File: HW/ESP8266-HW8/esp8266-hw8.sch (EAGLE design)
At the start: 28 parts, among them IC1 MCP1703CB, J2 Sensors2, J3 Analog, J4 Sensors1, J5 Enable, J6 PGM, J9 Pwr sw, T1 BSS138, U1 ESP07-16PIN, U2 2479

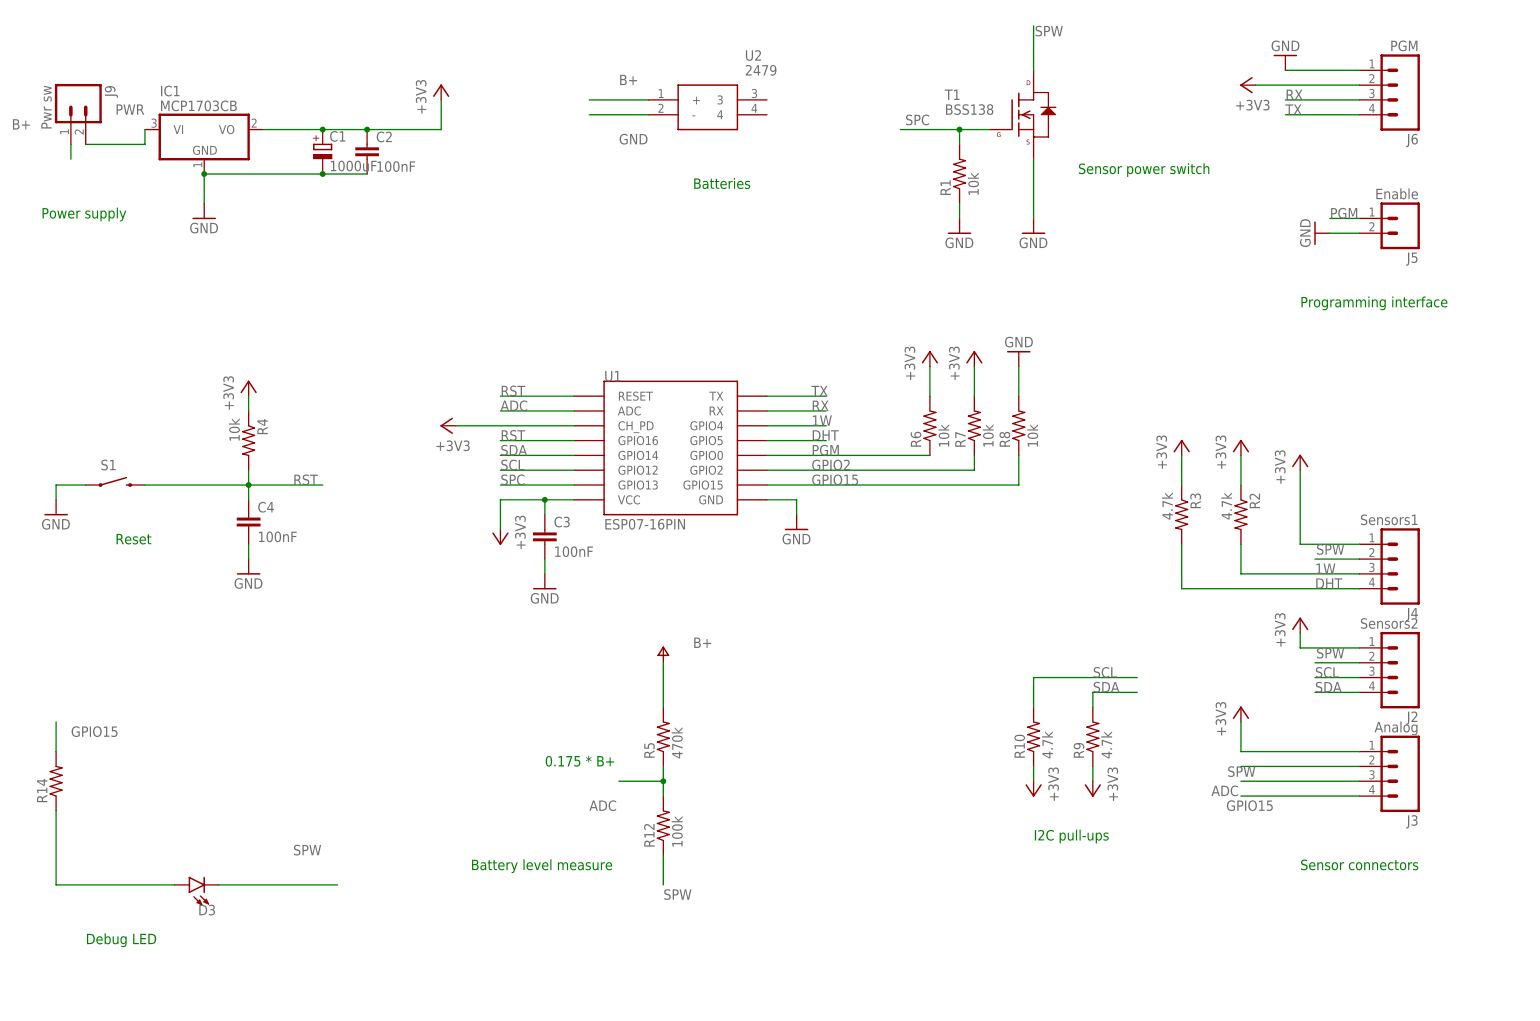
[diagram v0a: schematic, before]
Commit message: New pcb releases and some updated software
New (final?) releases of pcbs for version 7 and 8. New test program to run for test of the built hardware.
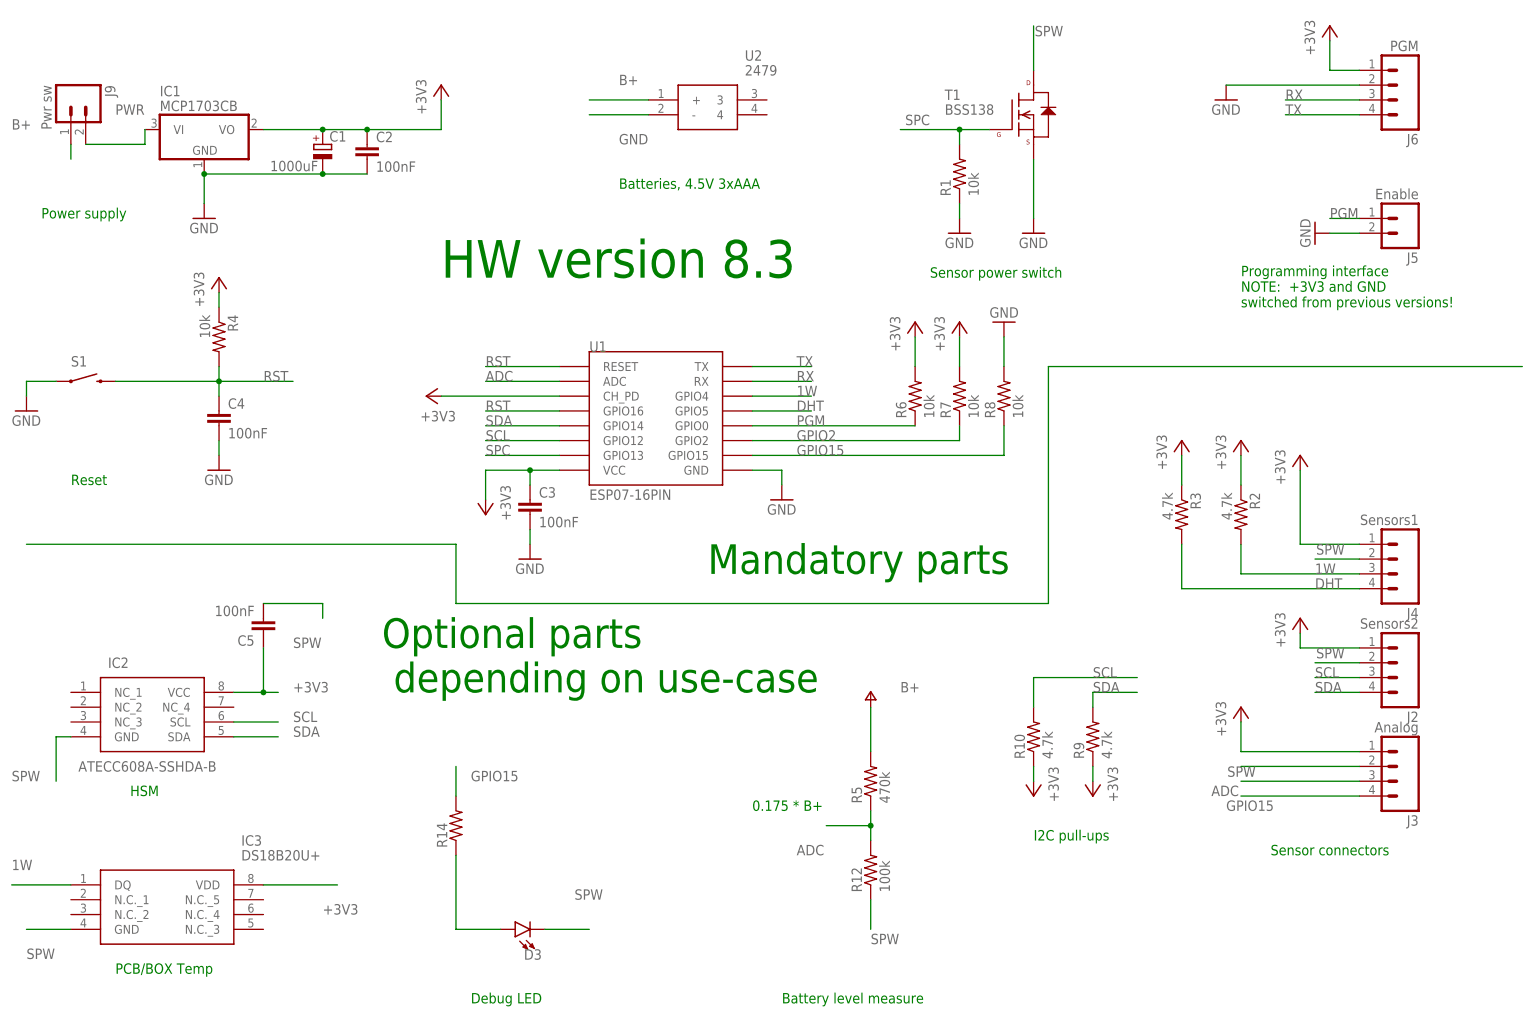
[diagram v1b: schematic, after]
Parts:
- added C5: 100nF, SparkFun-Passives:CAP0805
- added IC2: ATECC608A-SSHDA-B, SamacSys_Parts:ATECC608A-SSHDA-B
- added IC3: DS18B20U+, SamacSys_Parts:DS18B20U+
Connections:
- net +3V3: now also C5.1, IC2.VCC, IC3.VDD, J6.1; no longer J6.2
- net 1W: now also IC3.DQ
- net GND: now also J6.2; no longer J6.1
- net SCL: now also IC2.SCL
- net SDA: now also IC2.SDA
- net SPW: now also C5.2, IC2.GND, IC3.GND
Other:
- note added: "Batteries, 4.5V 3xAAA"
- note added: "HSM"
- note added: "HW version 8.3"
- note added: "Mandatory parts"
- note added: "Optional parts depending on use-case"
- note added: "PCB/BOX Temp"
- note added: "Programming interface NOTE: +3V3 and GND switched from previous versions!"
- note removed: "Batteries"
- note removed: "Programming interface"
- moved on the sheet: C3, C4, D3, R12, R14, R4, R5, R6, R7, R8, S1, U1
